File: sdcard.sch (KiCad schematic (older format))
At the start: 0 parts

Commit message: Add all POE logic with the si3404, schematic almost finished.
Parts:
- added J?: Micro_SD_Card_Det, symbol Micro_SD_Card_Det
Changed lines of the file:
@@
 LIBS:mpcie
 LIBS:si3406
+LIBS:si3404
+LIBS:SI-52003-F
+LIBS:ap2112
 LIBS:minipcie-eth-cache
 EELAYER 26 0
@@
 $Descr A4 11693 8268
 encoding utf-8
-Sheet 1 4
+Sheet 3 4
 Title ""
 Date ""
@@
 Comment4 ""
 $EndDescr
+$Comp
+L Micro_SD_Card_Det J?
+U 1 1 5BC4BC19
+P 2650 2590
+F 0 "J?" H 2600 1773 50  0000 C CNN
+F 1 "Micro_SD_Card_Det" H 2600 1864 50  0000 C CNN
+F 2 "" H 4700 3290 50  0001 C CNN
+F 3 "" H 2650 2690 50  0001 C CNN
+	1    2650 2590
+	-1   0    0    1
+$EndComp
 $EndSCHEMATC

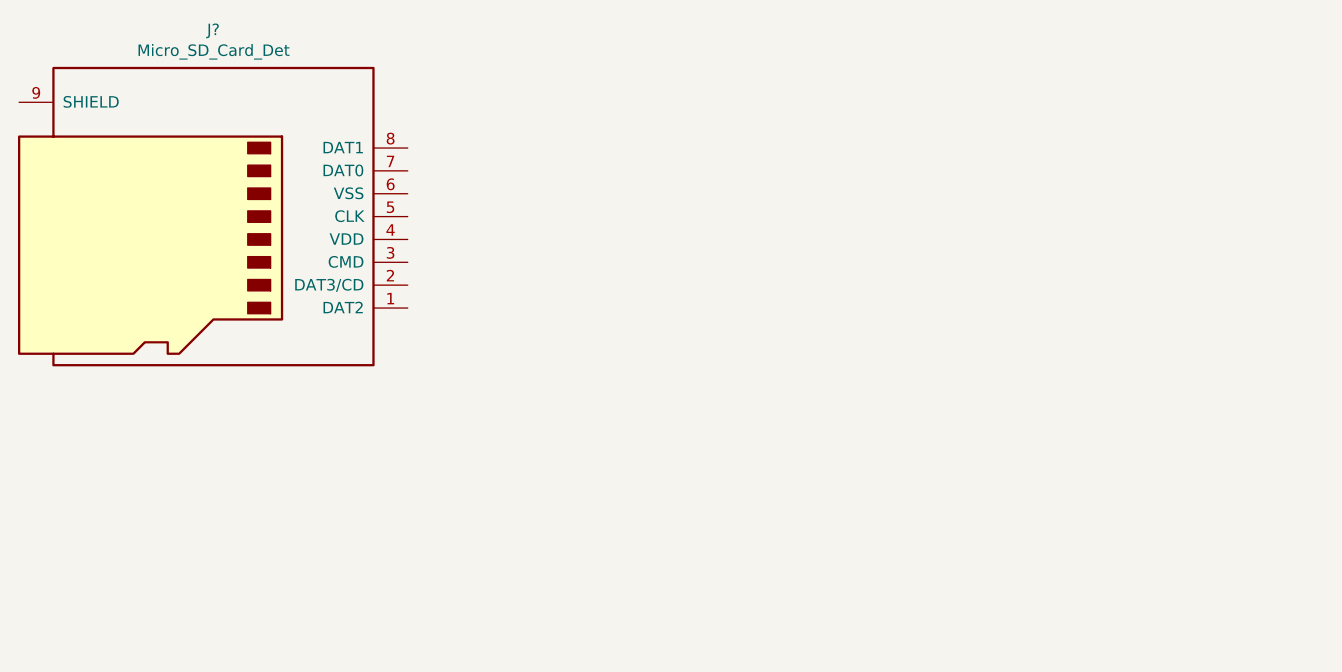
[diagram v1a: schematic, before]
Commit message: Added SDcard wiring
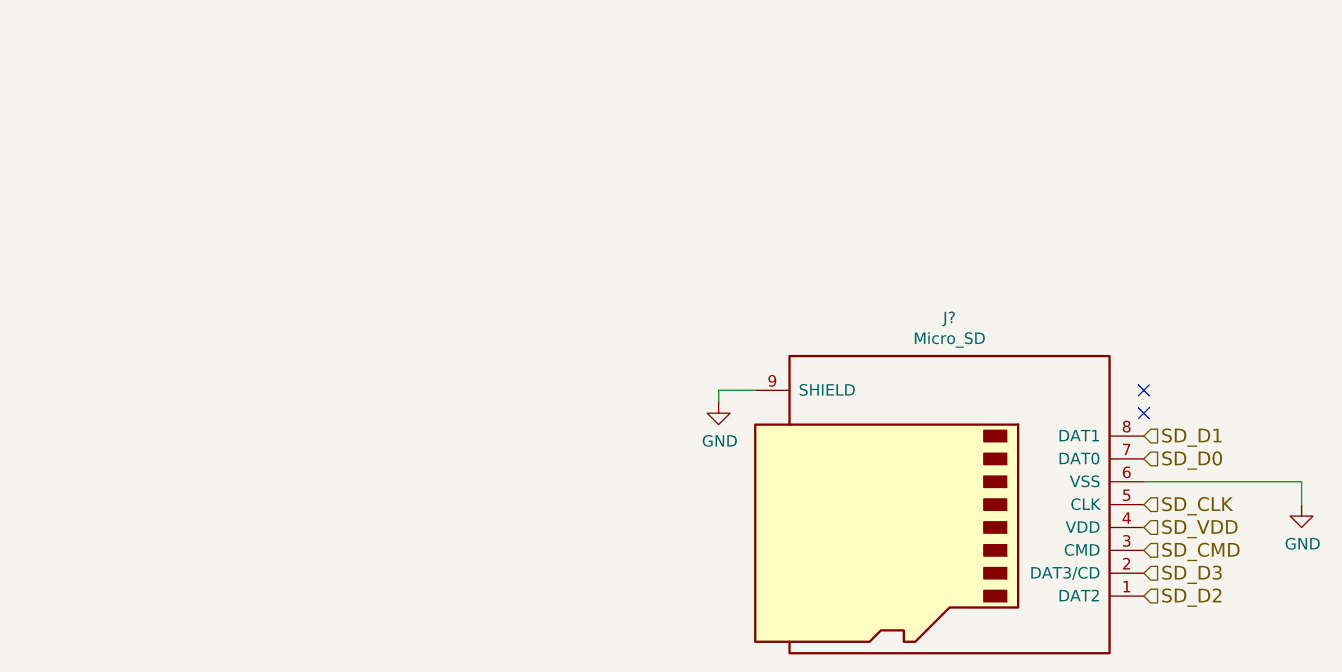
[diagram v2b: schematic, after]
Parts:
- J?: value Micro_SD_Card_Det -> Micro_SD
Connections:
- net SD_D2: now reaches J?.1 (DAT2)
- net SD_D3: now reaches J?.2 (DAT3/CD)
- net SD_CMD: now reaches J?.3 (CMD)
- net SD_VDD: now reaches J?.4 (VDD)
- net SD_CLK: now reaches J?.5 (CLK)
- net GND: now reaches J?.6 (VSS)
- net GND: now also J?.9 (SHIELD)
- net SD_D0: now reaches J?.7 (DAT0)
- net SD_D1: now reaches J?.8 (DAT1)
- no-connect marks 0 -> 2
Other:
- moved on the sheet: J?
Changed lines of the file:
@@
 $Descr A4 11693 8268
 encoding utf-8
-Sheet 3 4
+Sheet 4 4
 Title ""
 Date ""
@@
 L Micro_SD_Card_Det J?
 U 1 1 5BC4BC19
-P 2650 2590
-F 0 "J?" H 2600 1773 50  0000 C CNN
-F 1 "Micro_SD_Card_Det" H 2600 1864 50  0000 C CNN
-F 2 "" H 4700 3290 50  0001 C CNN
-F 3 "" H 2650 2690 50  0001 C CNN
-	1    2650 2590
+P 5870 3850
+F 0 "J?" H 5820 3033 50  0000 C CNN
+F 1 "Micro_SD" H 5820 3124 50  0000 C CNN
+F 2 "" H 7920 4550 50  0001 C CNN
+F 3 "" H 5870 3950 50  0001 C CNN
+	1    5870 3850
 	-1   0    0    1
 $EndComp
+Text HLabel 6770 3650 2    60   Input ~ 0
+SD_D0
+Text HLabel 6770 3550 2    60   Input ~ 0
+SD_D1
+Text HLabel 6770 4250 2    60   Input ~ 0
+SD_D2
+Text HLabel 6770 4150 2    60   Input ~ 0
+SD_D3
+Text HLabel 6770 4050 2    60   Input ~ 0
+SD_CMD
+Text HLabel 6770 3850 2    60   Input ~ 0
+SD_CLK
+NoConn ~ 6770 3450
+NoConn ~ 6770 3350
+Wire Wire Line
+	6770 3750 7460 3750
+Wire Wire Line
+	7460 3750 7460 3850
+$Comp
+L GND #PWR?
+U 1 1 5BC4DCD3
+P 7460 3850
+F 0 "#PWR?" H 7460 3600 50  0001 C CNN
+F 1 "GND" H 7465 3677 50  0000 C CNN
+F 2 "" H 7460 3850 50  0001 C CNN
+F 3 "" H 7460 3850 50  0001 C CNN
+	1    7460 3850
+	1    0    0    -1
+$EndComp
+Text HLabel 6770 3950 2    60   Input ~ 0
+SD_VDD
+Wire Wire Line
+	5070 3350 4910 3350
+Wire Wire Line
+	4910 3350 4910 3400
+$Comp
+L GND #PWR?
+U 1 1 5BC4DF1B
+P 4910 3400
+F 0 "#PWR?" H 4910 3150 50  0001 C CNN
+F 1 "GND" H 4915 3227 50  0000 C CNN
+F 2 "" H 4910 3400 50  0001 C CNN
+F 3 "" H 4910 3400 50  0001 C CNN
+	1    4910 3400
+	1    0    0    -1
+$EndComp
 $EndSCHEMATC

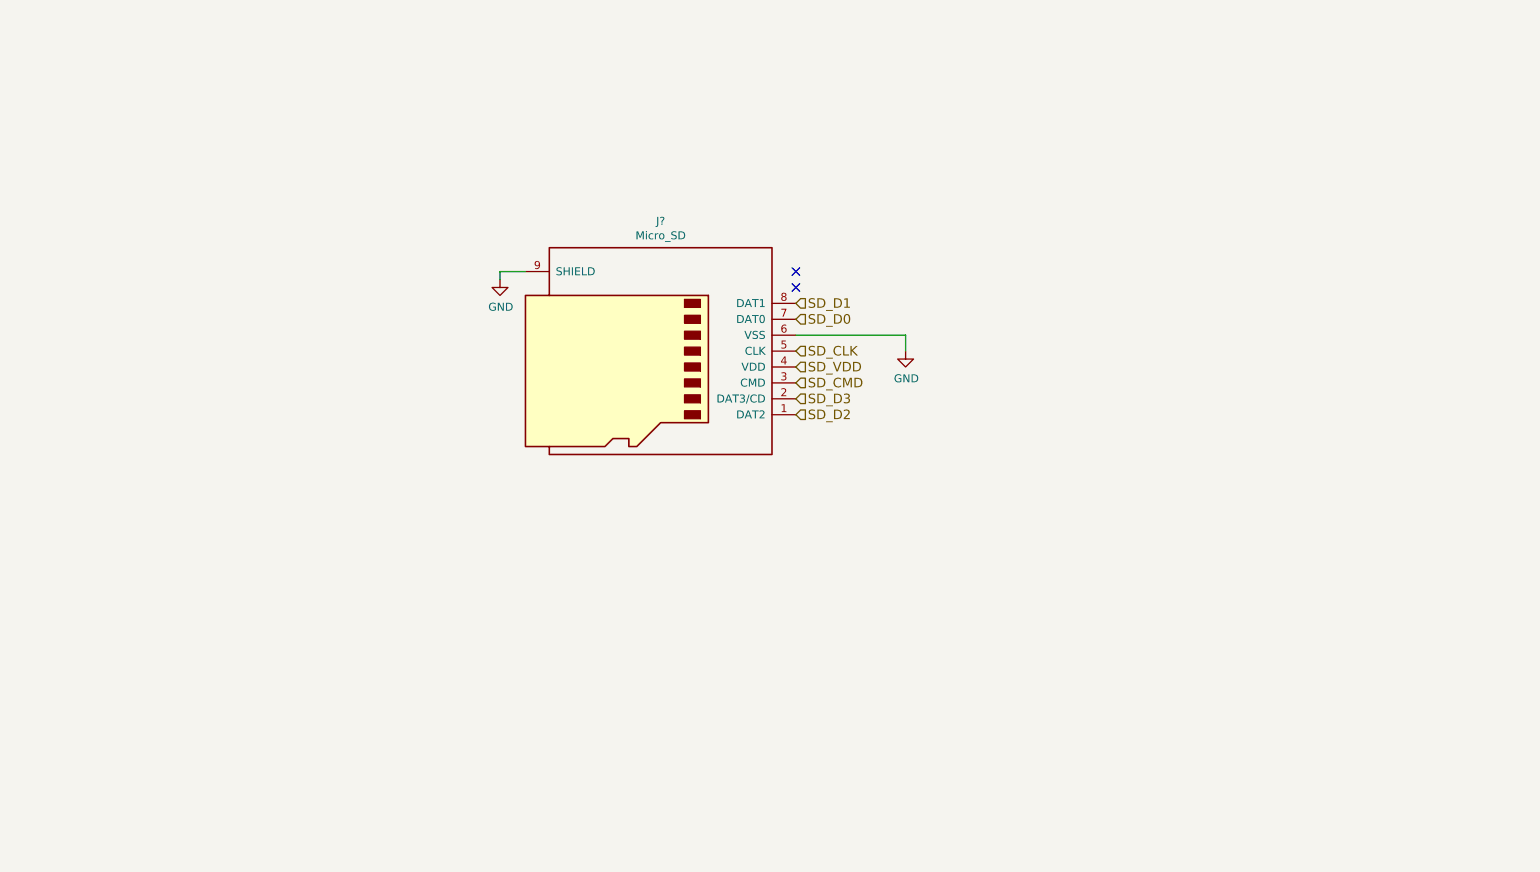
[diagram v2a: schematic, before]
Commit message: Rearrange components, validate package sizes, think about power plane placement since the ref design is 4 layers... can I add snubbers and other filtering and avoid 4-layer design?
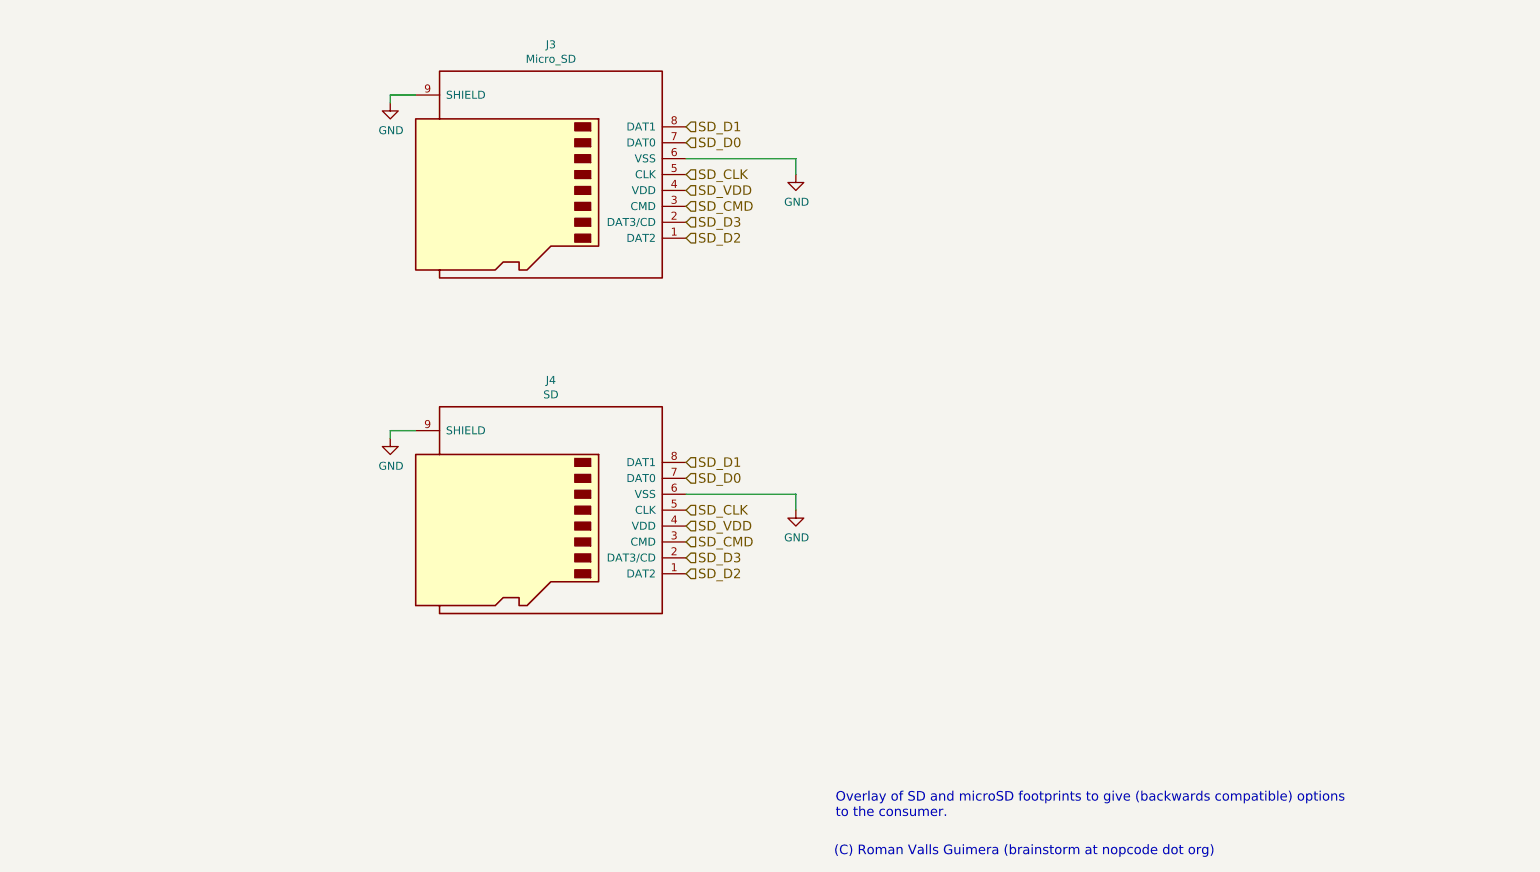
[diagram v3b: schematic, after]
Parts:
- added J4: SD, KiCad/Connect.pretty:microSD_Card_Receptacle_Wuerth_693072010801, symbol Micro_SD_Card_Det
- J3: renamed from J?; footprint (none) -> KiCad/Connect.pretty:SD_Card_Receptacle
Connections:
- net GND: now also J4.6 (VSS), J4.9 (SHIELD)
- net SD_CLK: now also J4.5 (CLK)
- net SD_CMD: now also J4.3 (CMD)
- net SD_D0: now also J4.7 (DAT0)
- net SD_D1: now also J4.8 (DAT1)
- net SD_D2: now also J4.1 (DAT2)
- net SD_D3: now also J4.2 (DAT3/CD)
- net SD_VDD: now also J4.4 (VDD)
- no-connect marks 2 -> 0
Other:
- note added: "(C) Roman Valls Guimera (brainstorm at nopcode dot org)"
- note added: "Overlay of SD and microSD footprints to give (backwards compatible) options \nto the consumer."
- moved on the sheet: J3
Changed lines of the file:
@@
 $EndDescr
 $Comp
-L Micro_SD_Card_Det J?
+L Micro_SD_Card_Det J3
 U 1 1 5BC4BC19
-P 5870 3850
-F 0 "J?" H 5820 3033 50  0000 C CNN
-F 1 "Micro_SD" H 5820 3124 50  0000 C CNN
-F 2 "" H 7920 4550 50  0001 C CNN
-F 3 "" H 5870 3950 50  0001 C CNN
-	1    5870 3850
+P 5180 2740
+F 0 "J3" H 5130 1923 50  0000 C CNN
+F 1 "Micro_SD" H 5130 2014 50  0000 C CNN
+F 2 "KiCad/Connect.pretty:SD_Card_Receptacle" H 7230 3440 50  0001 C CNN
+F 3 "" H 5180 2840 50  0001 C CNN
+	1    5180 2740
 	-1   0    0    1
 $EndComp
-Text HLabel 6770 3650 2    60   Input ~ 0
+Text HLabel 6080 2540 2    60   Input ~ 0
 SD_D0
-Text HLabel 6770 3550 2    60   Input ~ 0
+Text HLabel 6080 2440 2    60   Input ~ 0
 SD_D1
-Text HLabel 6770 4250 2    60   Input ~ 0
+Text HLabel 6080 3140 2    60   Input ~ 0
 SD_D2
-Text HLabel 6770 4150 2    60   Input ~ 0
+Text HLabel 6080 3040 2    60   Input ~ 0
 SD_D3
-Text HLabel 6770 4050 2    60   Input ~ 0
+Text HLabel 6080 2940 2    60   Input ~ 0
 SD_CMD
-Text HLabel 6770 3850 2    60   Input ~ 0
+Text HLabel 6080 2740 2    60   Input ~ 0
 SD_CLK
-NoConn ~ 6770 3450
-NoConn ~ 6770 3350
 Wire Wire Line
-	6770 3750 7460 3750
+	6080 2640 6770 2640
 Wire Wire Line
-	7460 3750 7460 3850
+	6770 2640 6770 2740
 $Comp
-L GND #PWR?
+L GND #PWR016
 U 1 1 5BC4DCD3
-P 7460 3850
-F 0 "#PWR?" H 7460 3600 50  0001 C CNN
-F 1 "GND" H 7465 3677 50  0000 C CNN
-F 2 "" H 7460 3850 50  0001 C CNN
-F 3 "" H 7460 3850 50  0001 C CNN
-	1    7460 3850
+P 6770 2740
+F 0 "#PWR016" H 6770 2490 50  0001 C CNN
+F 1 "GND" H 6775 2567 50  0000 C CNN
+F 2 "" H 6770 2740 50  0001 C CNN
+F 3 "" H 6770 2740 50  0001 C CNN
+	1    6770 2740
 	1    0    0    -1
 $EndComp
-Text HLabel 6770 3950 2    60   Input ~ 0
+Text HLabel 6080 2840 2    60   Input ~ 0
 SD_VDD
 Wire Wire Line
-	5070 3350 4910 3350
+	4380 2240 4220 2240
 Wire Wire Line
-	4910 3350 4910 3400
+	4220 2240 4220 2290
 $Comp
-L GND #PWR?
+L GND #PWR017
 U 1 1 5BC4DF1B
-P 4910 3400
-F 0 "#PWR?" H 4910 3150 50  0001 C CNN
-F 1 "GND" H 4915 3227 50  0000 C CNN
-F 2 "" H 4910 3400 50  0001 C CNN
-F 3 "" H 4910 3400 50  0001 C CNN
-	1    4910 3400
+P 4220 2290
+F 0 "#PWR017" H 4220 2040 50  0001 C CNN
+F 1 "GND" H 4225 2117 50  0000 C CNN
+F 2 "" H 4220 2290 50  0001 C CNN
+F 3 "" H 4220 2290 50  0001 C CNN
+	1    4220 2290
 	1    0    0    -1
 $EndComp
+$Comp
+L Micro_SD_Card_Det J4
+U 1 1 5BC34ECF
+P 5180 4850
+F 0 "J4" H 5130 4033 50  0000 C CNN
+F 1 "SD" H 5130 4124 50  0000 C CNN
+F 2 "KiCad/Connect.pretty:microSD_Card_Receptacle_Wuerth_693072010801" H 7230 5550 50  0001 C CNN
+F 3 "" H 5180 4950 50  0001 C CNN
+	1    5180 4850
+	-1   0    0    1
+$EndComp
+Text HLabel 6080 4650 2    60   Input ~ 0
+SD_D0
+Text HLabel 6080 4550 2    60   Input ~ 0
+SD_D1
+Text HLabel 6080 5250 2    60   Input ~ 0
+SD_D2
+Text HLabel 6080 5150 2    60   Input ~ 0
+SD_D3
+Text HLabel 6080 5050 2    60   Input ~ 0
+SD_CMD
+Text HLabel 6080 4850 2    60   Input ~ 0
+SD_CLK
+Wire Wire Line
+	6080 4750 6770 4750
+Wire Wire Line
+	6770 4750 6770 4850
+$Comp
+L GND #PWR018
+U 1 1 5BC34EE0
+P 6770 4850
+F 0 "#PWR018" H 6770 4600 50  0001 C CNN
+F 1 "GND" H 6775 4677 50  0000 C CNN
+F 2 "" H 6770 4850 50  0001 C CNN
+F 3 "" H 6770 4850 50  0001 C CNN
+	1    6770 4850
+	1    0    0    -1
+$EndComp
+Text HLabel 6080 4950 2    60   Input ~ 0
+SD_VDD
+Wire Wire Line
+	4380 4350 4220 4350
+Wire Wire Line
+	4220 4350 4220 4400
+$Comp
+L GND #PWR019
+U 1 1 5BC34EE9
+P 4220 4400
+F 0 "#PWR019" H 4220 4150 50  0001 C CNN
+F 1 "GND" H 4225 4227 50  0000 C CNN
+F 2 "" H 4220 4400 50  0001 C CNN
+F 3 "" H 4220 4400 50  0001 C CNN
+	1    4220 4400
+	1    0    0    -1
+$EndComp
+Text Notes 7020 6790 0    60   ~ 0
+Overlay of SD and microSD footprints to give (backwards compatible) options \nto the consumer.
+Text Notes 7010 7030 0    60   ~ 0
+(C) Roman Valls Guimera (brainstorm at nopcode dot org)
 $EndSCHEMATC

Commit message: Good discussion with Rob Powers about price margins for 2 layer PCB boards vs 4 layer PCBs... no market for that so closing this project and moving to a wESP32-based (or VoCore2) board :-S
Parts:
- removed J4: SD, KiCad/Connect.pretty:microSD_Card_Receptacle_Wuerth_693072010801, symbol Micro_SD_Card_Det
- J3: footprint KiCad/Connect.pretty:SD_Card_Receptacle -> KiCad/Connect.pretty:microSD_Card_Receptacle_Wuerth_693072010801
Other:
- note added: "Only microSD.\n"
- note removed: "Overlay of SD and microSD footprints to give (backwards compatible) options \nto the consumer."
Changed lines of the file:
@@
 F 0 "J3" H 5130 1923 50  0000 C CNN
 F 1 "Micro_SD" H 5130 2014 50  0000 C CNN
-F 2 "KiCad/Connect.pretty:SD_Card_Receptacle" H 7230 3440 50  0001 C CNN
+F 2 "KiCad/Connect.pretty:microSD_Card_Receptacle_Wuerth_693072010801" H 7230 3440 50  0001 C CNN
 F 3 "" H 5180 2840 50  0001 C CNN
 	1    5180 2740
@@
 	1    0    0    -1
 $EndComp
-$Comp
-L Micro_SD_Card_Det J4
-U 1 1 5BC34ECF
-P 5180 4850
-F 0 "J4" H 5130 4033 50  0000 C CNN
-F 1 "SD" H 5130 4124 50  0000 C CNN
-F 2 "KiCad/Connect.pretty:microSD_Card_Receptacle_Wuerth_693072010801" H 7230 5550 50  0001 C CNN
-F 3 "" H 5180 4950 50  0001 C CNN
-	1    5180 4850
-	-1   0    0    1
-$EndComp
-Text HLabel 6080 4650 2    60   Input ~ 0
-SD_D0
-Text HLabel 6080 4550 2    60   Input ~ 0
-SD_D1
-Text HLabel 6080 5250 2    60   Input ~ 0
-SD_D2
-Text HLabel 6080 5150 2    60   Input ~ 0
-SD_D3
-Text HLabel 6080 5050 2    60   Input ~ 0
-SD_CMD
-Text HLabel 6080 4850 2    60   Input ~ 0
-SD_CLK
-Wire Wire Line
-	6080 4750 6770 4750
-Wire Wire Line
-	6770 4750 6770 4850
-$Comp
-L GND #PWR018
-U 1 1 5BC34EE0
-P 6770 4850
-F 0 "#PWR018" H 6770 4600 50  0001 C CNN
-F 1 "GND" H 6775 4677 50  0000 C CNN
-F 2 "" H 6770 4850 50  0001 C CNN
-F 3 "" H 6770 4850 50  0001 C CNN
-	1    6770 4850
-	1    0    0    -1
-$EndComp
-Text HLabel 6080 4950 2    60   Input ~ 0
-SD_VDD
-Wire Wire Line
-	4380 4350 4220 4350
-Wire Wire Line
-	4220 4350 4220 4400
-$Comp
-L GND #PWR019
-U 1 1 5BC34EE9
-P 4220 4400
-F 0 "#PWR019" H 4220 4150 50  0001 C CNN
-F 1 "GND" H 4225 4227 50  0000 C CNN
-F 2 "" H 4220 4400 50  0001 C CNN
-F 3 "" H 4220 4400 50  0001 C CNN
-	1    4220 4400
-	1    0    0    -1
-$EndComp
 Text Notes 7020 6790 0    60   ~ 0
-Overlay of SD and microSD footprints to give (backwards compatible) options \nto the consumer.
+Only microSD.\n
 Text Notes 7010 7030 0    60   ~ 0
 (C) Roman Valls Guimera (brainstorm at nopcode dot org)
